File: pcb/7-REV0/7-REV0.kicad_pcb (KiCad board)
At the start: 4 copper layers, 80 x 80.2 mm, 227 parts, among them J201 Conn_01x03, J202 TYPE-C-31-M-12, J301 Conn_01x10, J302 Conn_01x09, Q202 MMBT7002K, Q300 SI2301, Q301 SI2301, Q302 SI2301, Q303 SI2301, Q304 SI2301, Q305 SI2301, Q306 SI2301, Q307 SI2301, Q401 BCM857, Q402 SI2301, Q601 MMDT3906, Q602 SI2301, SW101 SW_SPST, SW102 4P_button_sw, U102 W25Q128JVSIQ, U105 MT29F1G01ABAFDWB, U2 74LVC8T245BQ, U3 TLV74311PDBVR, U301 AiP74LVC1T45GC363.TR, U302 AiP74LVC1T45GC363.TR, U303 AiP74LVC1T45GC363.TR, U304 AiP74LVC1T45GC363.TR, U305 AiP74LVC1T45GC363.TR, U306 AiP74LVC1T45GC363.TR, U307 AiP74LVC1T45GC363.TR, U308 AiP74LVC1T45GC363.TR, U401 ME6211A33PG-N, U402 CD4067, U403 AP2127, U404 LMV321, U503 74HCT245BQ, U504 LMV324, U505 LMV324, U506 LMV321, U601 LMV321A, U602 LMV331, U603 LMV321, Y101 12Mhz

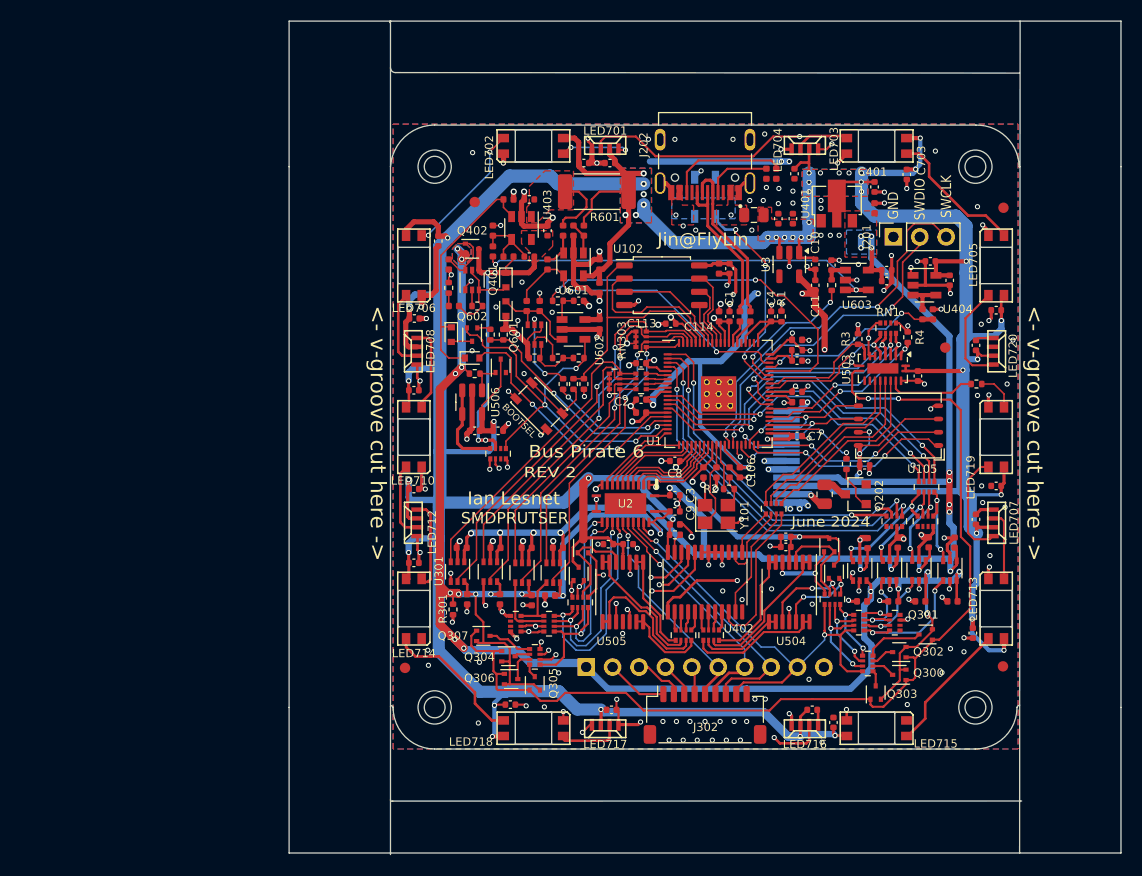
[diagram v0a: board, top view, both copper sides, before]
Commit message: remove old pullups, remove 1M pull-down. Add footprints and updated PCB.
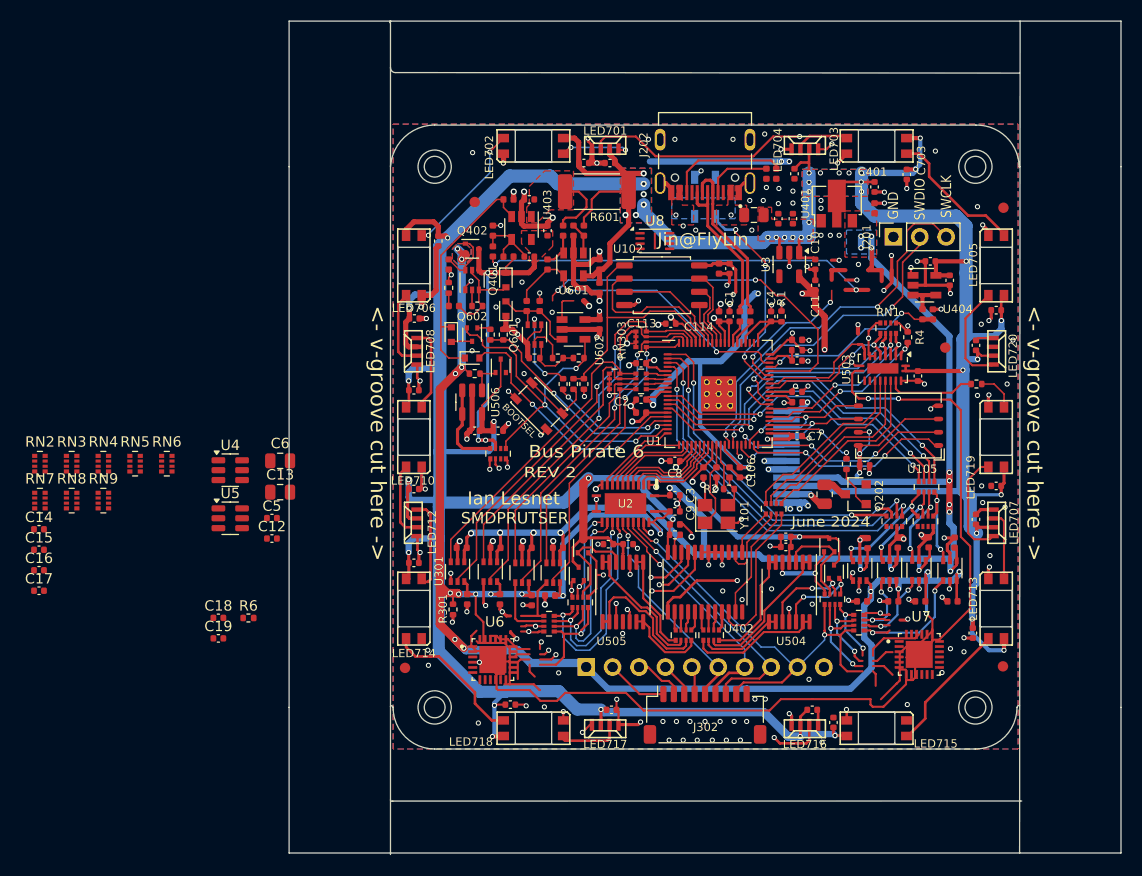
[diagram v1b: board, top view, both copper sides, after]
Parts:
- removed C413: 2.2uF, Capacitor_SMD:C_0402_1005Metric
- removed C414, C415, C416: 0.1uF, Capacitor_SMD:C_0402_1005Metric
- removed Q300, Q301, Q302, Q303, Q304, Q305, Q306, Q307: SI2301, Package_TO_SOT_SMD:SOT-523
- removed R3: 100K, Resistor_SMD:R_0402_1005Metric
- removed R414, R415: 10K, Resistor_SMD:R_0402_1005Metric
- removed RN304, RN310: 1M, Resistor_SMD:R_Array_Convex_4x0402
- removed RN311, RN312: 10K, Resistor_SMD:R_Array_Convex_4x0402
- removed U603: LMV321, Package_TO_SOT_SMD:SOT-23-5
- added C12: 0.1uF, Capacitor_SMD:C_0402_1005Metric, F.Cu at (88.2, 99.9)
- added C13: 10uF, Capacitor_SMD:C_0805_2012Metric, F.Cu at (89.0, 95.4)
- added C14: 0.1uF, Capacitor_SMD:C_0402_1005Metric, F.Cu at (65.8, 99.0)
- added C15: 0.1uF, Capacitor_SMD:C_0402_1005Metric, F.Cu at (65.8, 100.9)
- added C16: 0.1uF, Capacitor_SMD:C_0402_1005Metric, F.Cu at (65.8, 102.9)
- added C17: 0.1uF, Capacitor_SMD:C_0402_1005Metric, F.Cu at (65.8, 104.9)
- added C18: 0.1uF, Capacitor_SMD:C_0402_1005Metric, F.Cu at (83.1, 107.5)
- added C19: 2.2uF, Capacitor_SMD:C_0402_1005Metric, F.Cu at (83.1, 109.5)
- added C5: 0.1uF, Capacitor_SMD:C_0402_1005Metric, F.Cu at (88.2, 97.9)
- added C6: 10uF, Capacitor_SMD:C_0805_2012Metric, F.Cu at (89.0, 92.4)
- added R6: 100K, Resistor_SMD:R_0402_1005Metric, F.Cu at (86.0, 107.5)
- added RN2: 1M, Resistor_SMD:R_Array_Convex_4x0402, F.Cu at (65.9, 92.7)
- added RN3: 10K, Resistor_SMD:R_Array_Convex_4x0402, F.Cu at (69.0, 92.7)
- added RN4: 4.7K, Resistor_SMD:R_Array_Convex_4x0402, F.Cu at (72.0, 92.7)
- added RN5: 2.2K, Resistor_SMD:R_Array_Convex_4x0402, F.Cu at (75.1, 92.7)
- added RN6: 2.2K, Resistor_SMD:R_Array_Convex_4x0402, F.Cu at (78.1, 92.7)
- added RN7: 4.7K, Resistor_SMD:R_Array_Convex_4x0402, F.Cu at (65.9, 96.2)
- added RN8: 1M, Resistor_SMD:R_Array_Convex_4x0402, F.Cu at (69.0, 96.2)
- added RN9: 10K, Resistor_SMD:R_Array_Convex_4x0402, F.Cu at (72.0, 96.2)
- added U4: MCP4725xxx-xCH, Package_TO_SOT_SMD:SOT-23-6, F.Cu at (84.2, 93.3)
- added U5: MCP4725xxx-xCH, Package_TO_SOT_SMD:SOT-23-6, F.Cu at (84.2, 97.9)
- added U6: TCA6416RTWT, qfn24-4x4x50:QFN50P400X400X80-25N, F.Cu at (109.5, 111.5)
- added U7: TCA6416RTWT, qfn24-4x4x50:QFN50P400X400X80-25N, F.Cu at (150.5, 111.0)
- added U8: APS6404L-3SQR-ZR, Package_SON:Winbond_USON-8-1EP_3x2mm_P0.5mm_EP0.2x1.6mm, F.Cu at (125.1, 71.2)
- L201: value 1.5A -> CBW201209U300T
- Q402, Q602: value SI2301 -> BC2301T 2.8A
- SW101: value SW_SPST -> TS3425BA 098 2.5H 250gf
- SW102: value 4P_button_sw -> TS3315A 250gf 025
- U1: value ~ -> RP2350B
- U504, U505: value LMV324 -> GS324MT/TR
- U601: value LMV321A -> GS321A-TR
- U602: value LMV331 -> GSV331-TR
- Y101: value 12Mhz -> ABM8-272-T3
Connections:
- U1 pad 53: PULLUP_EN_3V3 -> unconnected-(U1-GPIO42_ADC2-Pad53)
- U1 pad 55: VREG_ADJ_MCU -> unconnected-(U1-GPIO44_ADC4-Pad55)
- U1 pad 56: CURRENT_ADJ_MCU -> unconnected-(U1-GPIO45_ADC5-Pad56)
- U503 pad 11: PULLUP_EN -> unconnected-(U503-B7-Pad11)
- U503 pad 9: PULLUP_EN_3V3 -> GND
- U602 pad 1: Net-(U602-+) -> CURRENT_ADJ_MCU
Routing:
- net unconnected-(U503-B7-Pad11): track 0.00 -> 97.0 mm, vias 0 -> 2
- net PULLUP_EN: track 97.0 -> 0.00 mm, vias 2 -> 0
- net unconnected-(U1-GPIO45_ADC5-Pad56): track 0.00 -> 36.8 mm, vias 0 -> 2
- net (no net): track 0.00 -> 36.3 mm
- net CURRENT_ADJ_MCU: track 36.8 -> 2.86 mm, vias 2 -> 0
- net unconnected-(U1-GPIO44_ADC4-Pad55): track 0.00 -> 13.6 mm, vias 0 -> 2
- net VREG_ADJ_MCU: track 13.6 -> 0.00 mm, vias 2 -> 0
- net PULLUP_EN_3V3: track 12.4 -> 0.00 mm
- net Net-(Q301-D): track 5.64 -> 0.00 mm
- net Net-(Q307-D): track 4.34 -> 0.00 mm
- net Net-(Q306-D): track 2.87 -> 0.00 mm
- net Net-(U602-+): track 2.86 -> 0.00 mm
- net Net-(U603-+): track 2.29 -> 0.00 mm
- net Net-(Q300-D): track 2.24 -> 0.00 mm
- net Net-(Q302-D): track 2.23 -> 0.00 mm
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
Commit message: partial move to dfn/qfn
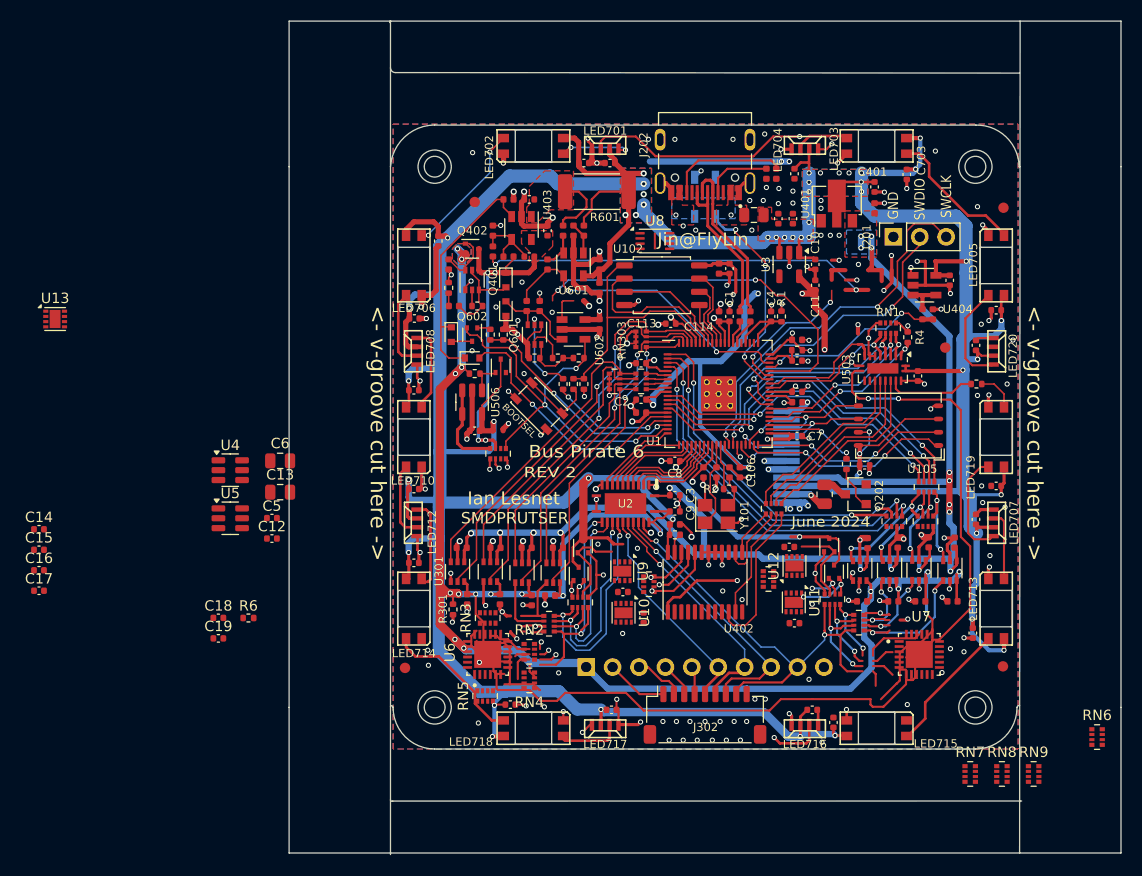
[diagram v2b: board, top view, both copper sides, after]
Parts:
- removed C405, C504: 2.2uF, Capacitor_SMD:C_0402_1005Metric
- removed U504, U505: GS324MT/TR, Package_SO:TSSOP-14_4.4x5mm_P0.65mm
- added U10: LM358_DFN, Package_DFN_QFN:DFN-8-1EP_2x2mm_P0.5mm_EP1.05x1.75mm, F.Cu at (122.1, 107.0)
- added U11: LM358_DFN, Package_DFN_QFN:DFN-8-1EP_2x2mm_P0.5mm_EP1.05x1.75mm, F.Cu at (138.4, 106.0)
- added U12: LM358_DFN, Package_DFN_QFN:DFN-8-1EP_2x2mm_P0.5mm_EP1.05x1.75mm, F.Cu at (138.5, 102.5)
- added U13: LM358_DFN, Package_DFN_QFN:DFN-8-1EP_2x2mm_P0.5mm_EP1.05x1.75mm, F.Cu at (67.4, 78.8)
- added U9: LM358_DFN, Package_DFN_QFN:DFN-8-1EP_2x2mm_P0.5mm_EP1.05x1.75mm, F.Cu at (121.9, 103.0)
- C507, C509: value 2.2uF -> 0.1uF
- moved RN7 93.2 mm to (155.4, 122.5)
- moved RN6 93.2 mm to (167.6, 119.0)
- moved RN8 93.2 mm to (158.4, 122.5)
- moved RN9 93.2 mm to (161.5, 122.5)
- moved RN2 50.4 mm to (113.0, 110.8)
- moved RN4 46.0 mm to (113.0, 113.5), turned to 180 degrees
- moved RN3 42.7 mm to (109.0, 107.5), turned to 90 degrees
- moved RN5 40.4 mm to (108.8, 115.0), turned to 90 degrees
- moved C507 8.34 mm to (138.5, 108.0)
- moved RN400 7.71 mm to (136.0, 103.8), turned to 0 degrees
- moved C510 7.24 mm to (124.0, 107.5), turned to -90 degrees
- moved RN401 5.92 mm to (124.5, 104.2), turned to 180 degrees
- moved C509 4.81 mm to (122.0, 105.0)
- moved U6 0.71 mm to (109.0, 111.0), turned to 90 degrees
- moved C508 0.33 mm to (138.0, 100.7), turned to 180 degrees
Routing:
- net unconnected-(U503-B7-Pad11): track 97.0 -> 0.00 mm, vias 2 -> 0
- net (no net): track 36.3 -> 129.0 mm, vias 0 -> 2
- net MUX_BPIO6: track 14.1 -> 0.00 mm
- net MUX_BPIO2: track 13.7 -> 0.00 mm
- net MUX_BPIO1: track 12.9 -> 0.00 mm
- net MUX_BPIO4: track 12.7 -> 0.00 mm
- net MUX_BPIO7: track 11.3 -> 0.00 mm
- net MUX_BPIO0: track 9.88 -> 0.00 mm
- net MUX_BPIO5: track 8.15 -> 0.00 mm
- net MUX_BPIO3: track 7.79 -> 0.00 mm
- net Net-(RN317B-R1.1): track 9.21 -> 3.92 mm
- net Net-(RN317D-R1.1): track 8.98 -> 4.75 mm, vias 2 -> 1
- net +VUSB: track 439.5 -> 435.2 mm
- net GND: track 199.6 -> 196.2 mm, vias 177 -> 174
- net BPIO7: track 44.4 -> 47.3 mm
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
